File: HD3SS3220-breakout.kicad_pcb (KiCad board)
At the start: 4 copper layers, 30.6 x 52.4 mm, 31 parts, among them J1 USB_C_Receptacle, J2 U-A-39SS-Y-1, J3 A2541WV-2x4P, SW1 SW_DIP_x04, U1 HD3SS3220RNHR, U2 TPD2EUSB30, U3 TPD4EUSB30, U4 HT7533-1_C14289

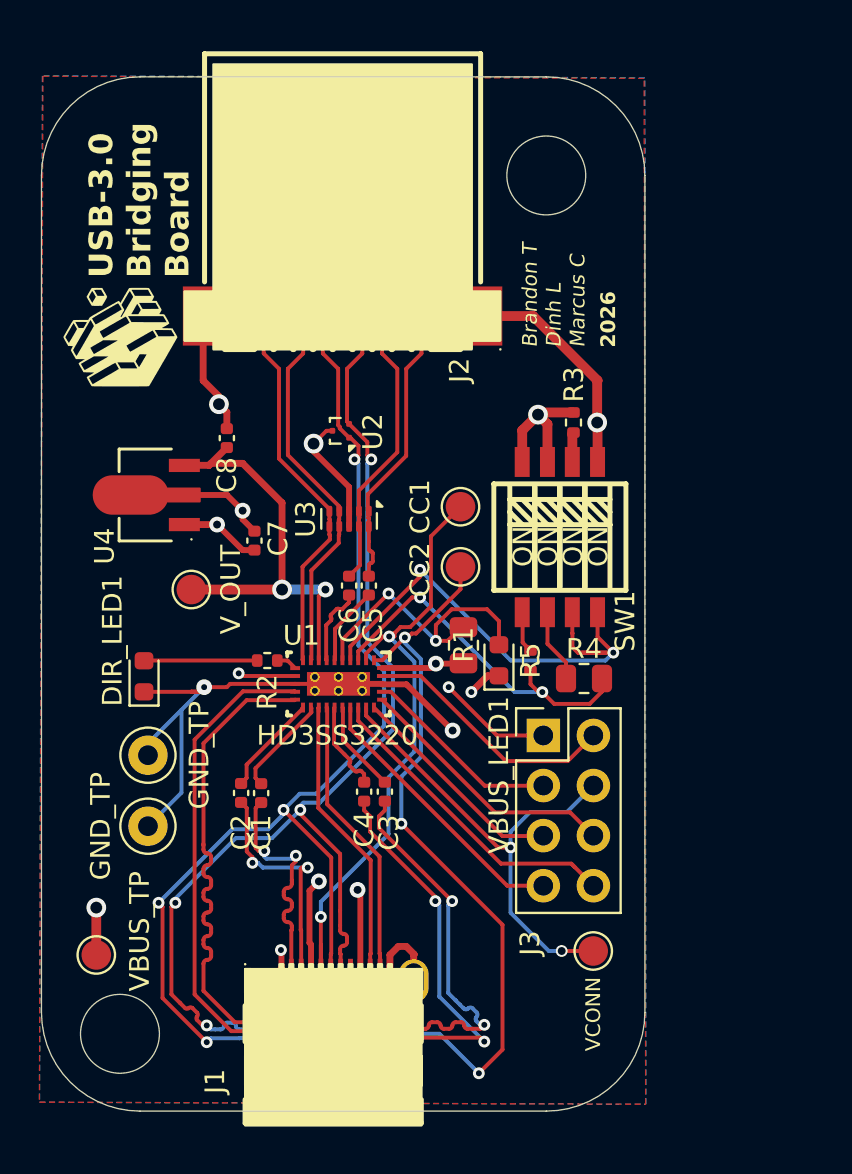
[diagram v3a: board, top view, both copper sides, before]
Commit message: Added missing components (Coupling capacitors and led resistors, wired board again
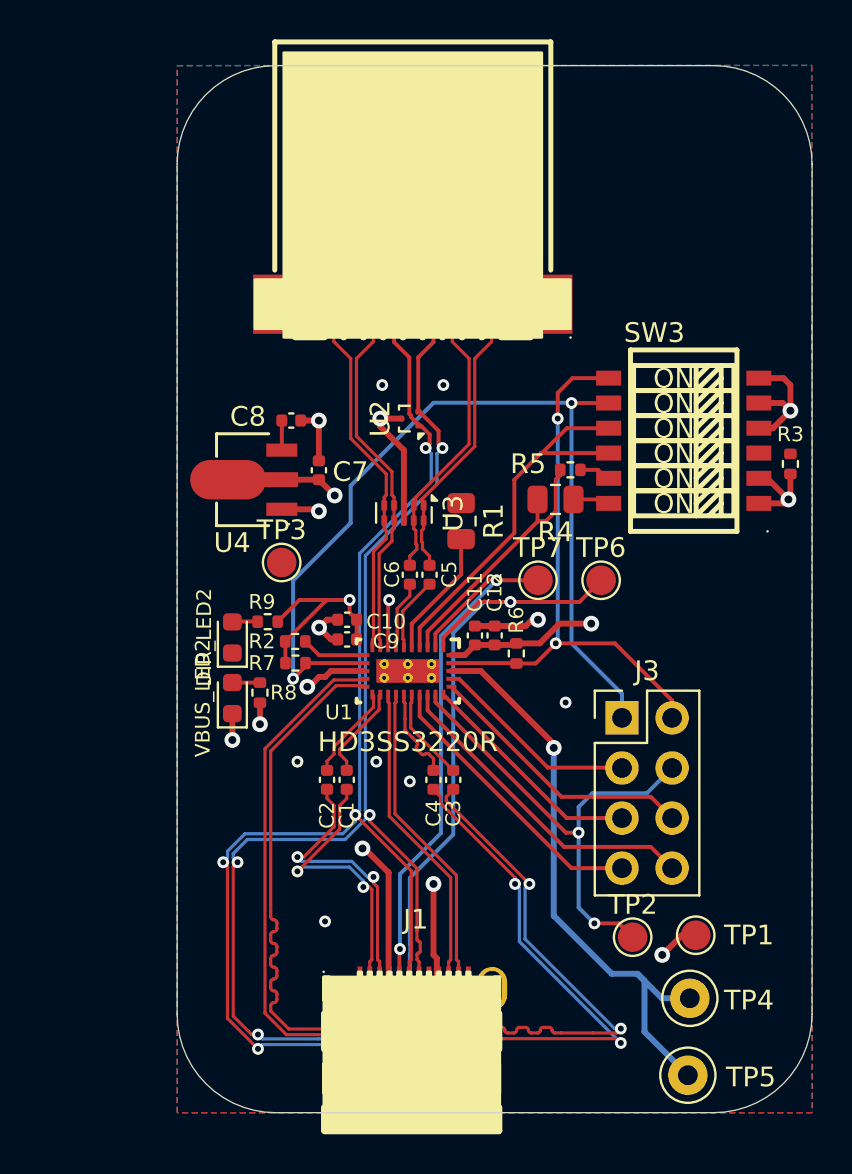
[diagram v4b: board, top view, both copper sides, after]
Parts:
- removed CC1: CC1, TestPoint:TestPoint_Pad_D1.5mm
- removed CC2: CC2, TestPoint:TestPoint_Pad_D1.5mm
- removed DIR_LED1, VBUS_LED1: LED, LED_SMD:LED_0603_1608Metric
- removed G***: LOGO, LOGO
- removed GND_TP: GND1, TestPoint:TestPoint_Keystone_5000-5004_Miniature
- removed GND_TP: GND2, TestPoint:TestPoint_Keystone_5000-5004_Miniature
- removed SW1: SW_DIP_x04, Button_Switch_SMD:SW4
- removed VBUS_TP: VBUS, TestPoint:TestPoint_Pad_D1.5mm
- removed VCONN: VCONN, TestPoint:TestPoint_Pad_D1.5mm
- removed V_OUT: VCC33, TestPoint:TestPoint_Pad_D1.5mm
- added C10: 1uF, Capacitor_SMD:C_0402_1005Metric, F.Cu at (101.9, 62.8)
- added C11: 100nF, Capacitor_SMD:C_0402_1005Metric, F.Cu at (108.4, 63.6)
- added C12: 100uF, Capacitor_SMD:C_0402_1005Metric, F.Cu at (109.4, 63.6)
- added C9: 100nF, Capacitor_SMD:C_0402_1005Metric, F.Cu at (101.9, 63.8)
- added DIR_LED2: LED, LED_SMD:LED_0603_1608Metric, F.Cu at (96.1, 63.7)
- added R6: 10K, Resistor_SMD:R_0402_1005Metric, F.Cu at (110.5, 64.5)
- added R7: 10K, Resistor_SMD:R_0402_1005Metric, F.Cu at (99.3, 65.0)
- added R8: 1k, Resistor_SMD:R_0402_1005Metric, F.Cu at (97.5, 66.5)
- added R9: 1k, Resistor_SMD:R_0402_1005Metric, F.Cu at (97.9, 62.9)
- added SW3: DSHP06TSGER_C3293146, UWReality_Labs:SW-SMD_12P-L9.2-W5.4-P1.27-LS8.5, F.Cu at (119.0, 53.7)
- added TP1: VBUS, TestPoint:TestPoint_Pad_D1.5mm, F.Cu at (119.6, 78.8)
- added TP2: VCONN, TestPoint:TestPoint_Pad_D1.5mm, F.Cu at (116.4, 78.9)
- added TP3: VCC33, TestPoint:TestPoint_Pad_D1.5mm, F.Cu at (98.6, 59.9)
- added TP4: GND1, TestPoint:TestPoint_Keystone_5000-5004_Miniature, F.Cu at (119.3, 82.0)
- added TP5: GND2, TestPoint:TestPoint_Keystone_5000-5004_Miniature, F.Cu at (119.2, 85.9)
- added TP6: CC2, TestPoint:TestPoint_Pad_D1.5mm, F.Cu at (114.8, 60.8)
- added TP7: CC1, TestPoint:TestPoint_Pad_D1.5mm, F.Cu at (111.6, 60.8)
- added VBUS_LED2: LED, LED_SMD:LED_0603_1608Metric, F.Cu at (96.1, 66.8)
- moved R3 11.2 mm to (124.4, 54.9), turned to 90 degrees
- moved R5 9.88 mm to (113.2, 55.2), turned to 180 degrees
- moved R4 9.20 mm to (112.5, 56.7), turned to 180 degrees
- moved R1 6.30 mm to (107.7, 57.8), turned to -90 degrees
- moved U4 5.00 mm to (97.2, 55.7)
- moved C7 4.84 mm to (100.5, 55.2), turned to 90 degrees
- moved C2 4.41 mm to (100.9, 70.9)
- moved C1 4.39 mm to (101.9, 70.9)
- moved J3 4.09 mm to (115.9, 67.8)
- moved J1 4.00 mm to (105.2, 83.5)
- moved J2 3.61 mm to (105.3, 47.1)
- moved U1 3.58 mm to (105.0, 65.4)
- moved C4 3.57 mm to (106.3, 70.9)
- moved U2 3.56 mm to (105.1, 52.6)
- moved C3 3.52 mm to (107.3, 70.9)
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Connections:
- net /Power Management, Configuration & Debug/ADDR renamed /ADDR
- net /Power Management, Configuration & Debug/ENn_CC renamed /ENn_CC
- net /Power Management, Configuration & Debug/ENn_Mux renamed /ENn_Mux
- net /Power Management, Configuration & Debug/ID renamed /ID
- net /Power Management, Configuration & Debug/INT_N renamed /INT_N
- net /Power Management, Configuration & Debug/MODE renamed /MODE
- net /Power Management, Configuration & Debug/SCL renamed /SCL
- net /Power Management, Configuration & Debug/SDA renamed /SDA
- net /Power Management, Configuration & Debug/VCONN renamed /VCONN
- net /Type-A Interface/D+ renamed /D+
- net /Type-A Interface/D- renamed /D-
- net /Type-A Interface/SSRX+ renamed /SSRX+
- net /Type-A Interface/SSRX- renamed /SSRX-
- net /Type-A Interface/SSTX+ renamed /SSTX+
- net /Type-A Interface/SSTX- renamed /SSTX-
- net /Type-C Interface & High-Speed Mux/CC1 renamed /CC1
- net /Type-C Interface & High-Speed Mux/CC2 renamed /CC2
- net /Type-C Interface & High-Speed Mux/RX1+ renamed /RX1+
- net /Type-C Interface & High-Speed Mux/RX1- renamed /RX1-
- net /Type-C Interface & High-Speed Mux/RX2+ renamed /RX2+
- net /Type-C Interface & High-Speed Mux/RX2- renamed /RX2-
- net /Type-C Interface & High-Speed Mux/SSTXMUX+ renamed /SSTXMUX+
- net /Type-C Interface & High-Speed Mux/SSTXMUX- renamed /SSTXMUX-
- net /Type-C Interface & High-Speed Mux/TX1+ renamed /TX1+
- net /Type-C Interface & High-Speed Mux/TX1- renamed /TX1-
- net /Type-C Interface & High-Speed Mux/TX1_IC+ renamed /TX1_IC+
- net /Type-C Interface & High-Speed Mux/TX1_IC- renamed /TX1_IC-
- net /Type-C Interface & High-Speed Mux/TX2+ renamed /TX2+
- net /Type-C Interface & High-Speed Mux/TX2- renamed /TX2-
- net /Type-C Interface & High-Speed Mux/TX2_IC+ renamed /TX2_IC+
- net /Type-C Interface & High-Speed Mux/TX2_IC- renamed /TX2_IC-
- net Net-(U1-DIR) renamed /DIR
- net Net-(U1-VBUS_DET) renamed /VBUS_DET
- C8 pad 1: /Power Management, Configuration & Debug/V_OUT -> /<NO NET>
- R2 pad 1: Net-(DIR_LED1-A) -> /<NO NET>
- U1 pad 4: /Power Management, Configuration & Debug/PORT -> /PORT
- U1 pad 8: /Power Management, Configuration & Debug/V_OUT -> /<NO NET>
- U4 pad 3: /Power Management, Configuration & Debug/V_OUT -> /<NO NET>
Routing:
- net /ENn_Mux: track 20.4 -> 47.3 mm
- net /Power Management, Configuration & Debug/PORT: track 25.9 -> 0.00 mm, vias 2 -> 0
- net /Power Management, Configuration & Debug/V_OUT: track 22.0 -> 0.00 mm, vias 2 -> 0
- net /PORT: track 0.00 -> 19.8 mm
- net /ENn_CC: track 13.1 -> 29.3 mm, vias 0 -> 2
- net /<NO NET>: track 0.00 -> 16.2 mm, vias 0 -> 2
- net GND: track 67.9 -> 58.9 mm, vias 10 -> 17
- net /VBUS_DET: track 15.0 -> 6.52 mm, vias 2 -> 0
- net Net-(DIR_LED1-A): track 5.75 -> 0.00 mm
- net /MODE: track 18.4 -> 13.1 mm, vias 2 -> 0
- net /TX2+: track 22.3 -> 27.3 mm
- net /TX2-: track 22.4 -> 27.3 mm
- net VBUS: track 40.7 -> 44.4 mm
- net /CC2: track 42.2 -> 39.2 mm, vias 4 -> 2
- net /D+: track 62.7 -> 65.4 mm
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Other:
- board size 30.6 x 52.4 mm -> 32.2 x 53.1 mm
- board text removed: "2026"
- board text removed: "Brandon T Dinh L Marcus C"
- board text removed: "USB-3.0 Bridging Board"

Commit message: Schematic Review: Removed Coupling Capacitors (no USB controller just mux)
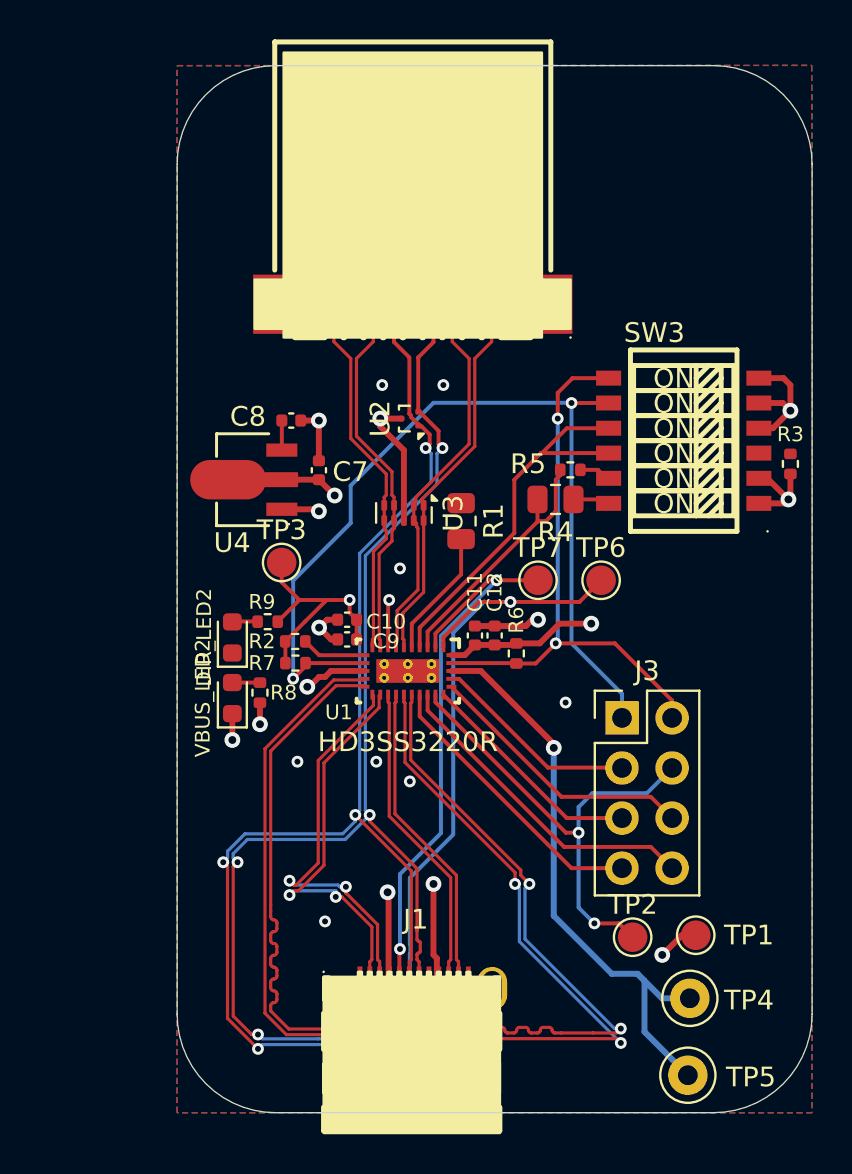
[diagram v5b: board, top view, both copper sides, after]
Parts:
- removed C1, C2, C3, C4, C5, C6: 100nF, Capacitor_SMD:C_0402_1005Metric
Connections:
- U1 pad 16: /TX1_IC- -> /TX1-
- U1 pad 17: /TX1_IC+ -> /TX1+
- U1 pad 20: /TX2_IC- -> /TX2-
- U1 pad 21: /TX2_IC+ -> /TX2+
- U1 pad 6: /SSTXMUX+ -> /SSTX+
- U1 pad 7: /SSTXMUX- -> /SSTX-
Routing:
- net /TX1-: track 14.0 -> 19.9 mm
- net /TX1+: track 14.1 -> 19.9 mm
- net /TX2-: track 27.3 -> 32.7 mm
- net /TX2+: track 27.3 -> 32.7 mm
- net /TX1_IC-: track 4.84 -> 0.00 mm
- net /TX1_IC+: track 4.84 -> 0.00 mm
- net /TX2_IC+: track 4.76 -> 0.00 mm
- net /TX2_IC-: track 4.74 -> 0.00 mm
- net /SSTX-: track 14.3 -> 18.8 mm
- net /SSTX+: track 14.3 -> 18.7 mm
- net /SSTXMUX+: track 3.78 -> 0.00 mm
- net /SSTXMUX-: track 3.49 -> 0.00 mm
- net /<NO NET>: track 16.2 -> 18.5 mm
- net VBUS: vias 9 -> 10
- net GND: vias 17 -> 18

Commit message: Rerouted for new elements added (5 DRC errors left)
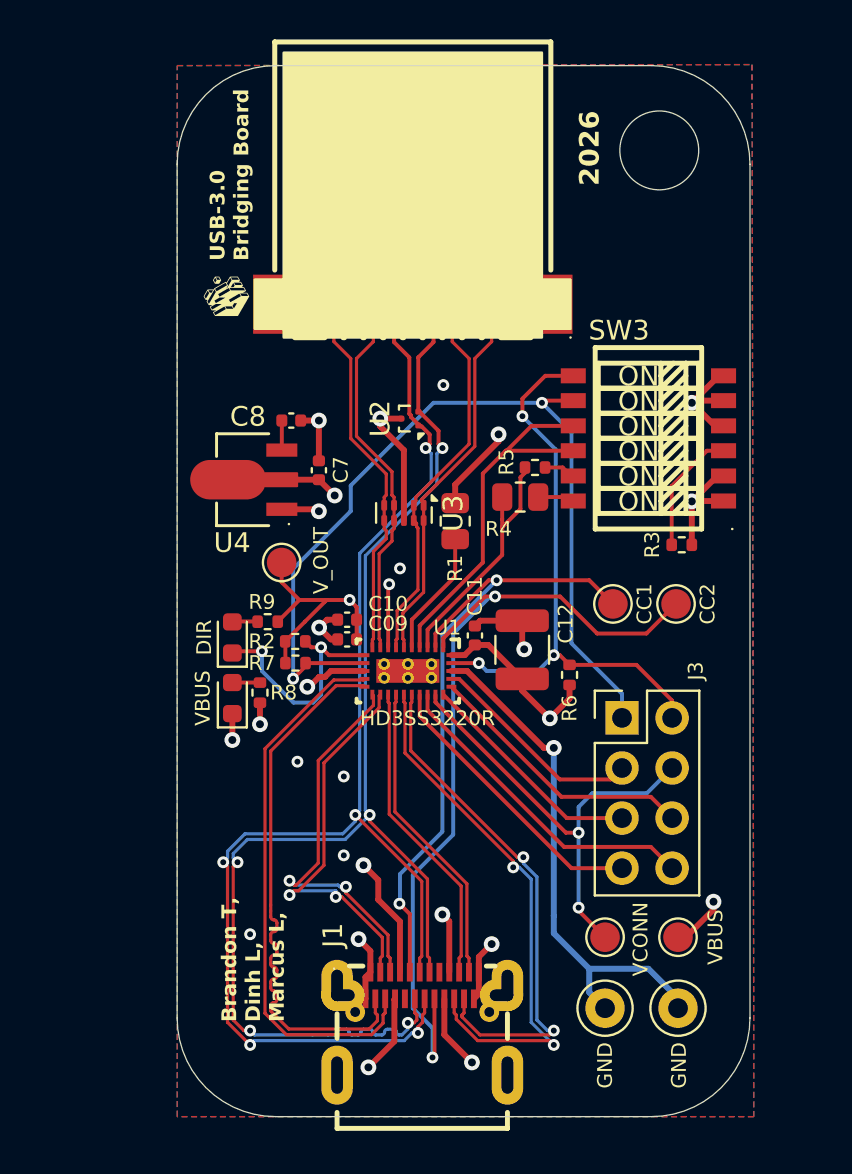
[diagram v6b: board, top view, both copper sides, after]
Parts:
- added G***: LOGO, LOGO, F.Cu at (95.8, 46.4)
- C12: footprint Capacitor_SMD:C_0402_1005Metric -> Capacitor_SMD:C_1210_3225Metric
- J1: footprint Interface_USB:USB-C-SMD_TYPE-C-USB-19 -> Interface_USB:USB-C-SMD_TYPEC-324G-BCP24
- moved R3 6.87 mm to (118.9, 59.0), turned to 180 degrees
- moved GND 5.40 mm to (115.0, 82.5)
- moved CC1 3.98 mm to (115.4, 62.0)
- moved CC2 3.98 mm to (118.6, 62.0)
- moved R6 2.91 mm to (113.2, 65.6), turned to 90 degrees
- moved R4 1.79 mm to (110.7, 56.6)
- moved R5 1.79 mm to (111.5, 55.1)
- moved SW3 1.79 mm to (117.2, 53.6)
- moved C12 1.58 mm to (110.8, 64.3)
- moved VCONN 1.40 mm to (115.0, 78.9)
- moved VBUS 0.91 mm to (118.7, 78.9)
- moved GND 0.78 mm to (118.7, 82.5)
- moved J1 0.56 mm to (105.7, 83.3)
- moved R1 0.30 mm to (107.4, 57.8)
- renumbered C9 to C09, TP7 to CC1, TP6 to CC2, DIR_LED2 to DIR, TP5 to GND, TP4 to GND, VBUS_LED2 to VBUS, TP1 to VBUS, TP2 to VCONN, TP3 to V_OUT
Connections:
- J1 pad : (no net) -> GND
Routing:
- net /DIR: track 3.29 -> 12.1 mm, vias 0 -> 2
- net Net-(SW3-A3): track 0.00 -> 6.35 mm
- net /TX2+: track 32.7 -> 26.5 mm
- net VBUS: track 44.4 -> 49.6 mm, vias 10 -> 11
- net /TX2-: track 32.7 -> 27.7 mm
- net /CC1: track 29.1 -> 33.4 mm
- net GND: track 58.9 -> 62.9 mm, vias 18 -> 17
- net /CC2: track 39.2 -> 43.2 mm
- net /<NO NET>: track 18.5 -> 19.7 mm
- net /ENn_Mux: track 47.3 -> 46.2 mm
- net /VCONN: track 24.2 -> 23.1 mm
- net /ENn_CC: track 29.3 -> 30.3 mm, vias 2 -> 3
- net /RX1-: track 27.2 -> 27.9 mm
- net /RX1+: track 27.1 -> 27.8 mm
- net /PORT: track 19.8 -> 19.2 mm
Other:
- board size 32.2 x 53.1 mm -> 29 x 53.3 mm
- board text added: "2026"
- board text added: "Brandon T, Dinh L, Marcus L,"
- board text added: "USB-3.0 Bridging Board"

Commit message: Rerouting PCB after fixes on schematic, fixed subsequent DRC errors
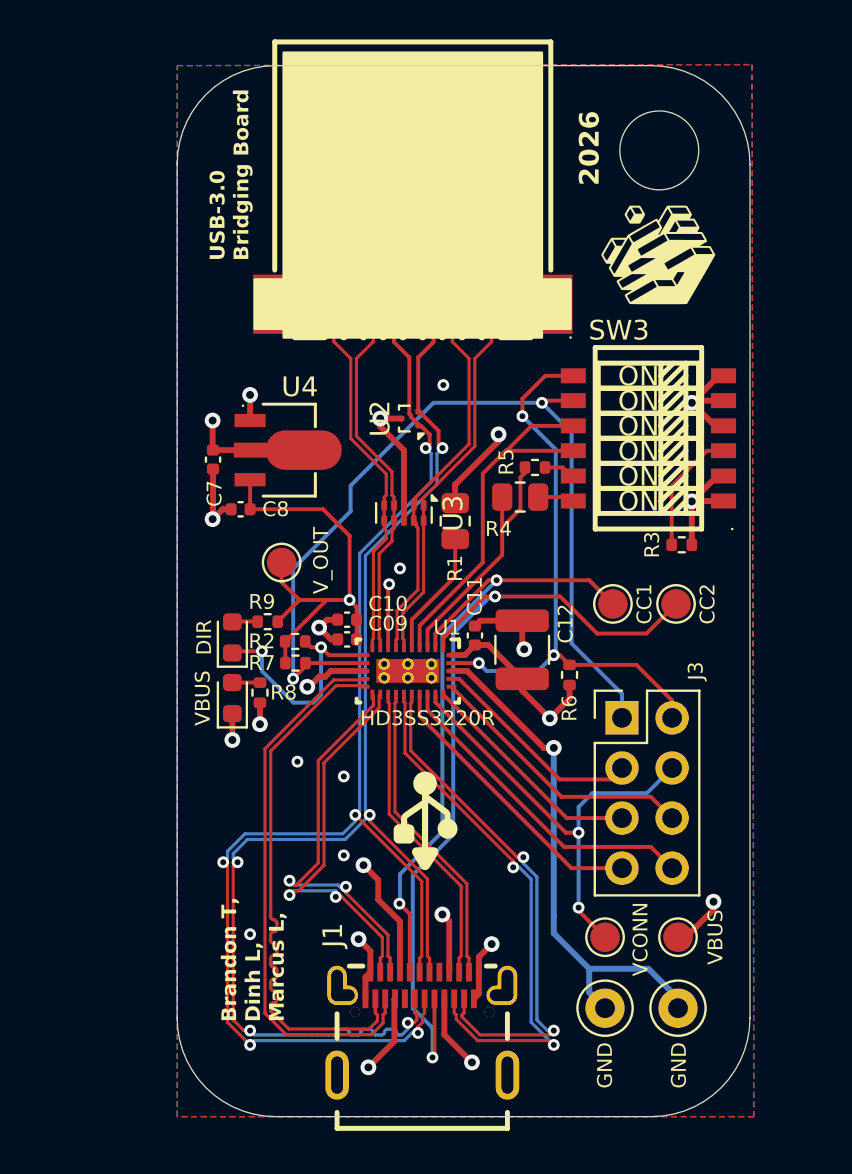
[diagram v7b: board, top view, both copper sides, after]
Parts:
- removed the G*** at (95.8, 46.4)
- added G***: LOGO, LOGO, F.Cu at (117.7, 44.3)
- added G***: LOGO, LOGO, F.Cu at (105.9, 73.0)
- moved C7 5.40 mm to (95.1, 54.7), turned to -90 degrees
- moved C8 5.18 mm to (96.5, 57.2), turned to 180 degrees
- moved U4 1.87 mm to (98.4, 54.2), turned to 180 degrees
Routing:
- net /<NO NET>: track 19.7 -> 28.5 mm
- net GND: track 62.9 -> 61.8 mm
